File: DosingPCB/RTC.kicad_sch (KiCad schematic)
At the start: 8 parts, among them SW5 SW_Push, U15 DS3231M

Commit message: Basically finished schematic
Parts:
- BT1: footprint (none) -> Battery:BatteryHolder_Keystone_3002_1x2032
- C8: renamed from C15; footprint (none) -> Capacitor_SMD:C_0603_1608Metric
- C9: renamed from C14; footprint (none) -> Capacitor_SMD:C_0603_1608Metric
- R10: renamed from R11; footprint (none) -> Resistor_SMD:R_0805_2012Metric
- R11: renamed from R13; footprint (none) -> Resistor_SMD:R_0805_2012Metric
- R9: renamed from R2; footprint (none) -> Resistor_SMD:R_0805_2012Metric
- SW3: renamed from SW5; footprint (none) -> Button_Switch_SMD:SW_SPST_TL3342
- renumbered U15 to U6
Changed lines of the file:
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@@
+	)
+	(junction
+		(at 142.24 86.36)
+		(diameter 0)
+		(color 0 0 0 0)
 	)
 	(junction
@@
 		(in_pos_files yes)
 		(dnp no)
-		(property "Reference" "C15"
+		(property "Reference" "C8"
 			(at 115.57 71.12 0)
 			(show_name no)
@@
 			)
 		)
-		(property "Footprint" ""
+		(property "Footprint" "Capacitor_SMD:C_0603_1608Metric"
 			(at 121.6152 74.93 0)
 			(hide yes)
@@
 			(project "DosingPCB"
 				(path "/3d87c741-aedb-4217-929e-9b442255b4c1/4f47eaf1-cd87-4360-81c9-dcb46df8285d"
-					(reference "C15")
+					(reference "C8")
 					(unit 1)
 				)
@@
 			)
 		)
-		(property "Footprint" ""
+		(property "Footprint" "Battery:BatteryHolder_Keystone_3002_1x2032"
 			(at 147.066 71.12 90)
 			(hide yes)
@@
 		(in_pos_files yes)
 		(dnp no)
-		(property "Reference" "SW5"
+		(property "Reference" "SW3"
 			(at 117.602 107.696 90)
 			(show_name no)
@@
 			)
 		)
-		(property "Footprint" ""
+		(property "Footprint" "Button_Switch_SMD:SW_SPST_TL3342"
 			(at 124.46 109.22 0)
 			(hide yes)
@@
 			(project "DosingPCB"
 				(path "/3d87c741-aedb-4217-929e-9b442255b4c1/4f47eaf1-cd87-4360-81c9-dcb46df8285d"
-					(reference "SW5")
+					(reference "SW3")
 					(unit 1)
 				)
@@
 		(in_pos_files yes)
 		(dnp no)
-		(property "Reference" "R11"
+		(property "Reference" "R10"
 			(at 123.698 92.71 0)
 			(show_name no)
@@
 			)
 		)
-		(property "Footprint" ""
+		(property "Footprint" "Resistor_SMD:R_0805_2012Metric"
 			(at 120.142 91.44 90)
 			(hide yes)
@@
 			(project "DosingPCB"
 				(path "/3d87c741-aedb-4217-929e-9b442255b4c1/4f47eaf1-cd87-4360-81c9-dcb46df8285d"
-					(reference "R11")
+					(reference "R10")
 					(unit 1)
 				)
@@
 		(dnp no)
 		(fields_autoplaced yes)
-		(property "Reference" "#PWR091"
+		(property "Reference" "#PWR040"
 			(at 151.13 85.09 0)
 			(hide yes)
@@
 			(project "DosingPCB"
 				(path "/3d87c741-aedb-4217-929e-9b442255b4c1/4f47eaf1-cd87-4360-81c9-dcb46df8285d"
-					(reference "#PWR091")
+					(reference "#PWR040")
+					(unit 1)
+				)
+			)
+		)
+	)
+	(symbol
+		(lib_id "power:PWR_FLAG")
+		(at 142.24 86.36 270)
+		(unit 1)
+		(body_style 1)
+		(exclude_from_sim no)
+		(in_bom yes)
+		(on_board yes)
+		(in_pos_files yes)
+		(dnp no)
+		(fields_autoplaced yes)
+		(property "Reference" "#FLG02"
+			(at 144.145 86.36 0)
+			(hide yes)
+			(show_name no)
+			(do_not_autoplace no)
+			(effects
+				(font
+					(size 1.27 1.27)
+				)
+			)
+		)
+		(property "Value" "PWR_FLAG"
+			(at 146.05 86.3599 90)
+			(show_name no)
+			(do_not_autoplace no)
+			(effects
+				(font
+					(size 1.27 1.27)
+				)
+				(justify left)
+			)
+		)
+		(property "Footprint" ""
+			(at 142.24 86.36 0)
+			(hide yes)
+			(show_name no)
+			(do_not_autoplace no)
+			(effects
+				(font
+					(size 1.27 1.27)
+				)
+			)
+		)
+		(property "Datasheet" ""
+			(at 142.24 86.36 0)
+			(hide yes)
+			(show_name no)
+			(do_not_autoplace no)
+			(effects
+				(font
+					(size 1.27 1.27)
+				)
+			)
+		)
+		(property "Description" "Special symbol for telling ERC where power comes from"
+			(at 142.24 86.36 0)
+			(hide yes)
+			(show_name no)
+			(do_not_autoplace no)
+			(effects
+				(font
+					(size 1.27 1.27)
+				)
+			)
+		)
+		(pin "1"
+		)
+		(instances
+			(project "DosingPCB"
+				(path "/3d87c741-aedb-4217-929e-9b442255b4c1/4f47eaf1-cd87-4360-81c9-dcb46df8285d"
+					(reference "#FLG02")
 					(unit 1)
 				)
@@
 		(in_pos_files yes)
 		(dnp no)
-		(property "Reference" "R13"
+		(property "Reference" "R11"
 			(at 167.132 94.742 0)
 			(show_name no)
@@
 			)
 		)
-		(property "Footprint" ""
+		(property "Footprint" "Resistor_SMD:R_0805_2012Metric"
 			(at 162.052 93.98 90)
 			(hide yes)
@@
 			(project "DosingPCB"
 				(path "/3d87c741-aedb-4217-929e-9b442255b4c1/4f47eaf1-cd87-4360-81c9-dcb46df8285d"
-					(reference "R13")
+					(reference "R11")
 					(unit 1)
 				)
@@
 		(dnp no)
 		(fields_autoplaced yes)
-		(property "Reference" "#PWR080"
+		(property "Reference" "#PWR039"
 			(at 142.24 120.65 0)
 			(hide yes)
@@
 			(project "DosingPCB"
 				(path "/3d87c741-aedb-4217-929e-9b442255b4c1/4f47eaf1-cd87-4360-81c9-dcb46df8285d"
-					(reference "#PWR080")
+					(reference "#PWR039")
 					(unit 1)
 				)
@@
 		(dnp no)
 		(fields_autoplaced yes)
-		(property "Reference" "#PWR081"
+		(property "Reference" "#PWR037"
 			(at 120.65 81.28 0)
 			(hide yes)
@@
 			(project "DosingPCB"
 				(path "/3d87c741-aedb-4217-929e-9b442255b4c1/4f47eaf1-cd87-4360-81c9-dcb46df8285d"
-					(reference "#PWR081")
+					(reference "#PWR037")
 					(unit 1)
 				)
@@
 		(in_pos_files yes)
 		(dnp no)
-		(property "Reference" "R2"
+		(property "Reference" "R9"
 			(at 117.094 88.9 0)
 			(show_name no)
@@
 			)
 		)
-		(property "Footprint" ""
+		(property "Footprint" "Resistor_SMD:R_0805_2012Metric"
 			(at 113.792 87.63 90)
 			(hide yes)
@@
 			(project "DosingPCB"
 				(path "/3d87c741-aedb-4217-929e-9b442255b4c1/4f47eaf1-cd87-4360-81c9-dcb46df8285d"
-					(reference "R2")
+					(reference "R9")
 					(unit 1)
 				)
@@
 		(in_pos_files yes)
 		(dnp no)
-		(property "Reference" "#PWR026"
+		(property "Reference" "#PWR036"
 			(at 120.65 71.12 0)
 			(hide yes)
@@
 			(project "DosingPCB"
 				(path "/3d87c741-aedb-4217-929e-9b442255b4c1/4f47eaf1-cd87-4360-81c9-dcb46df8285d"
-					(reference "#PWR026")
+					(reference "#PWR036")
 					(unit 1)
 				)
@@
 		(dnp no)
 		(fields_autoplaced yes)
-		(property "Reference" "U15"
+		(property "Reference" "U6"
 			(at 144.3833 106.68 0)
 			(show_name no)
@@
 			(project "DosingPCB"
 				(path "/3d87c741-aedb-4217-929e-9b442255b4c1/4f47eaf1-cd87-4360-81c9-dcb46df8285d"
-					(reference "U15")
+					(reference "U6")
 					(unit 1)
 				)
@@
 		(in_pos_files yes)
 		(dnp no)
-		(property "Reference" "#PWR011"
+		(property "Reference" "#PWR038"
 			(at 139.7 85.09 0)
 			(hide yes)
@@
 			(project "DosingPCB"
 				(path "/3d87c741-aedb-4217-929e-9b442255b4c1/4f47eaf1-cd87-4360-81c9-dcb46df8285d"
-					(reference "#PWR011")
+					(reference "#PWR038")
 					(unit 1)
 				)
@@
 		(in_pos_files yes)
 		(dnp no)
-		(property "Reference" "C14"
+		(property "Reference" "C9"
 			(at 145.542 75.438 90)
 			(show_name no)
@@
 			)
 		)
-		(property "Footprint" ""
+		(property "Footprint" "Capacitor_SMD:C_0603_1608Metric"
 			(at 143.51 79.7052 0)
 			(hide yes)
@@
 			(project "DosingPCB"
 				(path "/3d87c741-aedb-4217-929e-9b442255b4c1/4f47eaf1-cd87-4360-81c9-dcb46df8285d"
-					(reference "C14")
+					(reference "C9")
 					(unit 1)
 				)

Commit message: Starting Board setup
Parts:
- C8, C9: value 104uF -> .1uF
- SW3: footprint Button_Switch_SMD:SW_SPST_TL3342 -> Button_Switch_SMD:SW_Push_SPST_NO_3x4mm_Smart_E2
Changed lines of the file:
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@@
 			)
 		)
-		(property "Value" "104uF"
+		(property "Value" ".1uF"
 			(at 126.492 71.12 0)
 			(show_name no)
@@
 			)
 		)
-		(property "Footprint" "Button_Switch_SMD:SW_SPST_TL3342"
+		(property "Footprint" "Button_Switch_SMD:SW_Push_SPST_NO_3x4mm_Smart_E2"
 			(at 124.46 109.22 0)
 			(hide yes)
@@
 			)
 		)
-		(property "Value" "104uF"
+		(property "Value" ".1uF"
 			(at 146.05 82.296 90)
 			(show_name no)

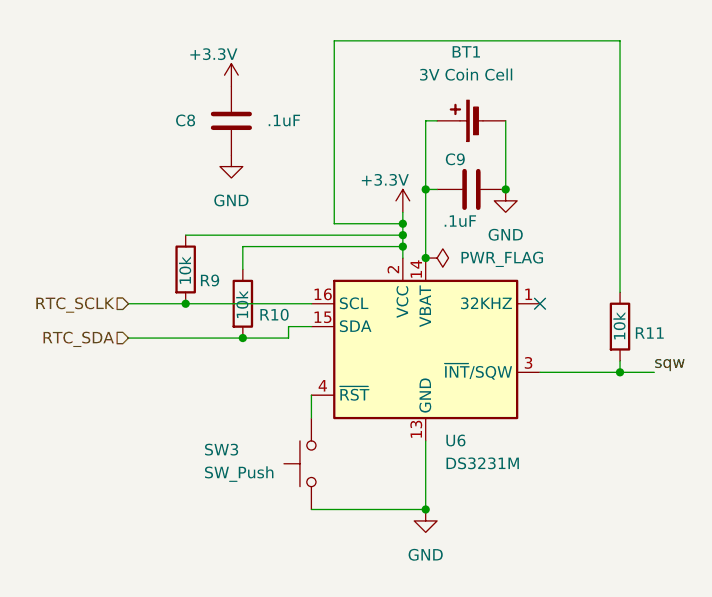
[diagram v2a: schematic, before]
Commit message: Quick RTC fix
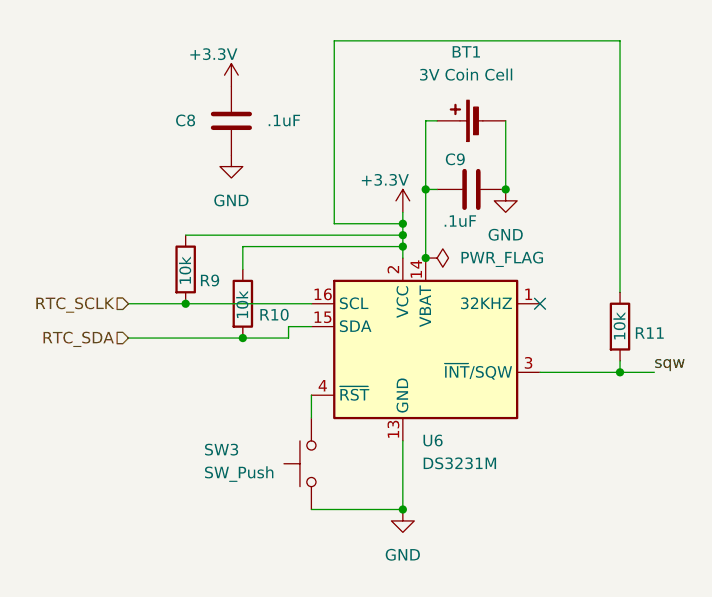
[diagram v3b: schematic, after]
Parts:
- removed U6: DS3231M, Package_SO:SOIC-16W_7.5x10.3mm_P1.27mm, symbol Timer_RTC:DS3231M
- added U6: DS3231M, Package_SO:SOIC-16W_7.5x10.3mm_P1.27mm, symbol RealTC:DS3231M
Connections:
- net +3.3V: now also U6.2 (VCC)
- net GND: now also U6.13 (GND)
- net RTC_SCLK: now also U6.16 (SCL)
- net RTC_SDA: now also U6.15 (SDA)
- net sqw: now also U6.3 (~{INT}/SQW)
- net at BT1.1 (+), C9.2: now also U6.14 (VBAT)
- net at SW3.2: now also U6.4 (~{RST})
- new net: U6.10 (GND), U6.11 (GND), U6.12 (GND), U6.5 (GND), U6.6 (GND), U6.7 (GND), U6.8 (GND), U6.9 (GND)
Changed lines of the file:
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@@
-	)
-	(junction
-		(at 142.24 114.3)
-		(diameter 0)
-		(color 0 0 0 0)
 	)
 	(junction
@@
 	)
 	(junction
+		(at 139.7 114.3)
+		(diameter 0)
+		(color 0 0 0 0)
+	)
+	(junction
 		(at 139.7 82.55)
 		(diameter 0)
@@
 	(wire
 		(pts
-			(xy 142.24 106.68) (xy 142.24 114.3)
-		)
-		(stroke
-			(width 0)
-			(type default)
-		)
-	)
-	(wire
-		(pts
 			(xy 121.92 85.09) (xy 139.7 85.09)
 		)
@@
 	(wire
 		(pts
+			(xy 139.7 106.68) (xy 139.7 114.3)
+		)
+		(stroke
+			(width 0)
+			(type default)
+		)
+	)
+	(wire
+		(pts
 			(xy 139.7 83.82) (xy 139.7 85.09)
 		)
@@
 	(wire
 		(pts
-			(xy 142.24 114.3) (xy 129.54 114.3)
-		)
-		(stroke
-			(width 0)
-			(type default)
-		)
-	)
-	(wire
-		(pts
 			(xy 109.22 91.44) (xy 115.57 91.44)
 		)
@@
 		(pts
 			(xy 115.57 91.44) (xy 129.54 91.44)
+		)
+		(stroke
+			(width 0)
+			(type default)
+		)
+	)
+	(wire
+		(pts
+			(xy 139.7 114.3) (xy 129.54 114.3)
 		)
 		(stroke
@@
 	)
 	(symbol
+		(lib_id "RealTC:DS3231M")
+		(at 142.24 96.52 0)
+		(unit 1)
+		(body_style 1)
+		(exclude_from_sim no)
+		(in_bom yes)
+		(on_board yes)
+		(in_pos_files yes)
+		(dnp no)
+		(fields_autoplaced yes)
+		(property "Reference" "U6"
+			(at 141.8433 106.68 0)
+			(show_name no)
+			(do_not_autoplace no)
+			(effects
+				(font
+					(size 1.27 1.27)
+				)
+				(justify left)
+			)
+		)
+		(property "Value" "DS3231M"
+			(at 141.8433 109.22 0)
+			(show_name no)
+			(do_not_autoplace no)
+			(effects
+				(font
+					(size 1.27 1.27)
+				)
+				(justify left)
+			)
+		)
+		(property "Footprint" "Package_SO:SOIC-16W_7.5x10.3mm_P1.27mm"
+			(at 142.24 111.76 0)
+			(hide yes)
+			(show_name no)
+			(do_not_autoplace no)
+			(effects
+				(font
+					(size 1.27 1.27)
+				)
+			)
+		)
+		(property "Datasheet" "http://datasheets.maximintegrated.com/en/ds/DS3231.pdf"
+			(at 149.098 95.25 0)
+			(hide yes)
+			(show_name no)
+			(do_not_autoplace no)
+			(effects
+				(font
+					(size 1.27 1.27)
+				)
+			)
+		)
+		(property "Description" "Extremely Accurate I2C-Integrated RTC/TCXO/Crystal SOIC-16"
+			(at 142.24 96.52 0)
+			(hide yes)
+			(show_name no)
+			(do_not_autoplace no)
+			(effects
+				(font
+					(size 1.27 1.27)
+				)
+			)
+		)
+		(pin "6"
+		)
+		(pin "14"
+		)
+		(pin "12"
+		)
+		(pin "1"
+		)
+		(pin "10"
+		)
+		(pin "16"
+		)
+		(pin "11"
+		)
+		(pin "3"
+		)
+		(pin "13"
+		)
+		(pin "15"
+		)
+		(pin "4"
+		)
+		(pin "9"
+		)
+		(pin "2"
+		)
+		(pin "5"
+		)
+		(pin "7"
+		)
+		(pin "8"
+		)
+		(instances
+			(project "DosingPCB"
+				(path "/3d87c741-aedb-4217-929e-9b442255b4c1/4f47eaf1-cd87-4360-81c9-dcb46df8285d"
+					(reference "U6")
+					(unit 1)
+				)
+			)
+		)
+	)
+	(symbol
 		(lib_id "power:GND")
-		(at 142.24 114.3 0)
+		(at 139.7 114.3 0)
 		(unit 1)
 		(body_style 1)
@@
 		(fields_autoplaced yes)
 		(property "Reference" "#PWR039"
-			(at 142.24 120.65 0)
+			(at 139.7 120.65 0)
 			(hide yes)
 			(show_name no)
@@
 		)
 		(property "Value" "GND"
-			(at 142.24 119.38 0)
+			(at 139.7 119.38 0)
 			(show_name no)
 			(do_not_autoplace no)
@@
 		)
 		(property "Footprint" ""
-			(at 142.24 114.3 0)
+			(at 139.7 114.3 0)
 			(hide yes)
 			(show_name no)
@@
 		)
 		(property "Datasheet" ""
-			(at 142.24 114.3 0)
+			(at 139.7 114.3 0)
 			(hide yes)
 			(show_name no)
@@
 		)
 		(property "Description" "Power symbol creates a global label with name \"GND\" , ground"
-			(at 142.24 114.3 0)
+			(at 139.7 114.3 0)
 			(hide yes)
 			(show_name no)
@@
 					(unit 1)
 				)
-			)
-		)
-	)
-	(symbol
-		(lib_id "Timer_RTC:DS3231M")
-		(at 142.24 96.52 0)
-		(unit 1)
-		(body_style 1)
-		(exclude_from_sim no)
-		(in_bom yes)
-		(on_board yes)
-		(in_pos_files yes)
-		(dnp no)
-		(fields_autoplaced yes)
-		(property "Reference" "U6"
-			(at 144.3833 106.68 0)
-			(show_name no)
-			(do_not_autoplace no)
-			(effects
-				(font
-					(size 1.27 1.27)
-				)
-				(justify left)
-			)
-		)
-		(property "Value" "DS3231M"
-			(at 144.3833 109.22 0)
-			(show_name no)
-			(do_not_autoplace no)
-			(effects
-				(font
-					(size 1.27 1.27)
-				)
-				(justify left)
-			)
-		)
-		(property "Footprint" "Package_SO:SOIC-16W_7.5x10.3mm_P1.27mm"
-			(at 142.24 111.76 0)
-			(hide yes)
-			(show_name no)
-			(do_not_autoplace no)
-			(effects
-				(font
-					(size 1.27 1.27)
-				)
-			)
-		)
-		(property "Datasheet" "http://datasheets.maximintegrated.com/en/ds/DS3231.pdf"
-			(at 149.098 95.25 0)
-			(hide yes)
-			(show_name no)
-			(do_not_autoplace no)
-			(effects
-				(font
-					(size 1.27 1.27)
-				)
-			)
-		)
-		(property "Description" "Extremely Accurate I2C-Integrated RTC/TCXO/Crystal SOIC-16"
-			(at 142.24 96.52 0)
-			(hide yes)
-			(show_name no)
-			(do_not_autoplace no)
-			(effects
-				(font
-					(size 1.27 1.27)
-				)
-			)
-		)
-		(pin "13"
-		)
-		(pin "10"
-		)
-		(pin "12"
-		)
-		(pin "15"
-		)
-		(pin "3"
-		)
-		(pin "16"
-		)
-		(pin "1"
-		)
-		(pin "2"
-		)
-		(pin "5"
-		)
-		(pin "6"
-		)
-		(pin "8"
-		)
-		(pin "11"
-		)
-		(pin "7"
-		)
-		(pin "4"
-		)
-		(pin "9"
-		)
-		(pin "14"
-		)
-		(instances
-			(project "DosingPCB"
-				(path "/3d87c741-aedb-4217-929e-9b442255b4c1/4f47eaf1-cd87-4360-81c9-dcb46df8285d"
-					(reference "U6")
-					(unit 1)
-				)

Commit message: 98% completed PCB
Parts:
- SW3: footprint Button_Switch_SMD:SW_Push_SPST_NO_3x4mm_Smart_E2 -> Button_Switch_SMD:SW_Push_SPST_NO_Alps_SKRK
